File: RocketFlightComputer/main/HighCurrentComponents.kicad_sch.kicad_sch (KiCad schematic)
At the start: 31 parts, among them J1 BATT, Q2 SI2302, Q3 SI2302, Q4 SI2302

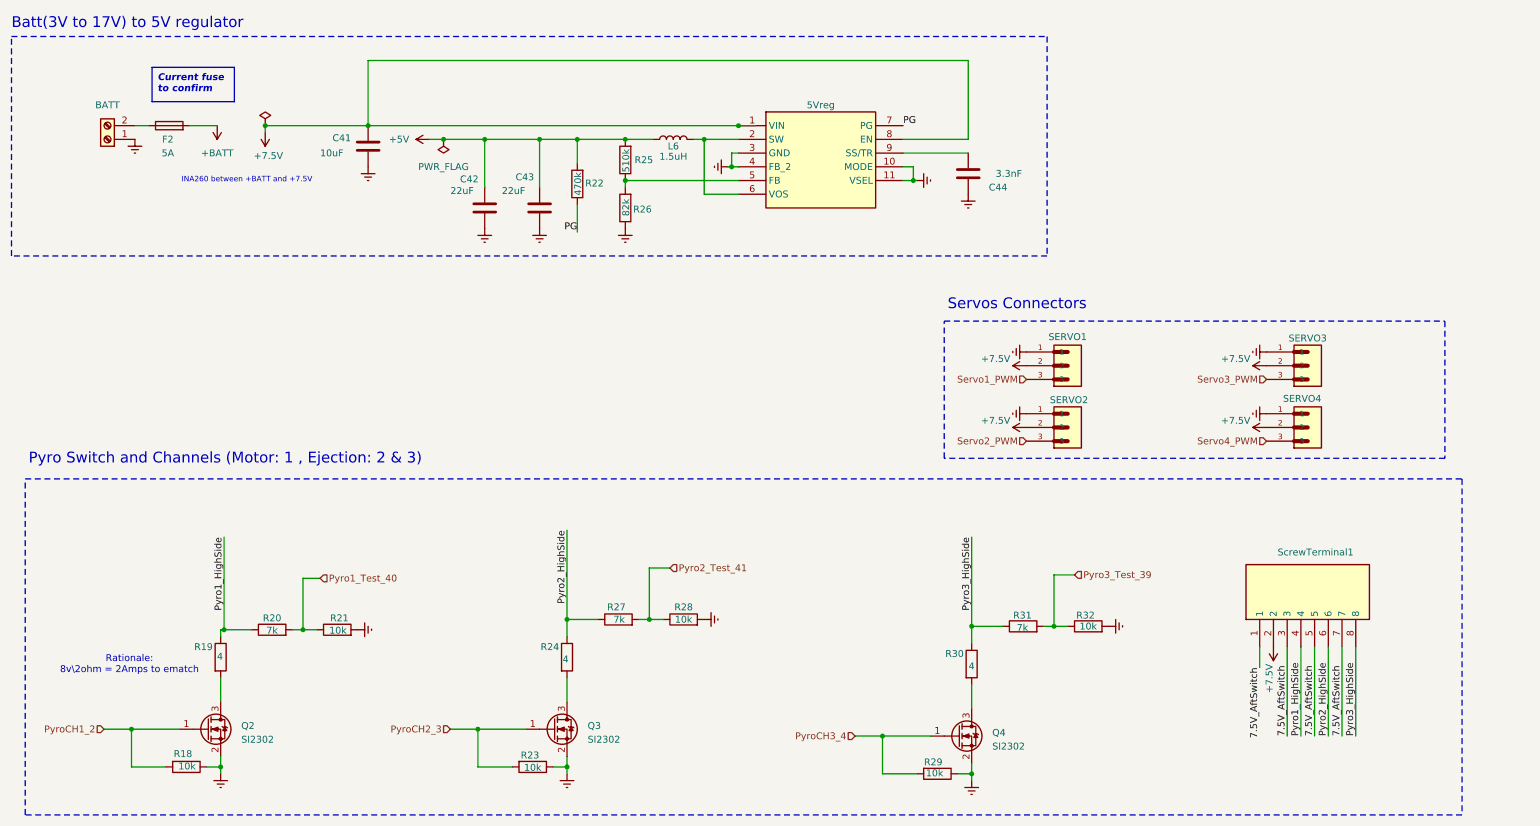
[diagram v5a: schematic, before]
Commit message: Addition of teensy example and milestone on routing completed, missing a few components to connect
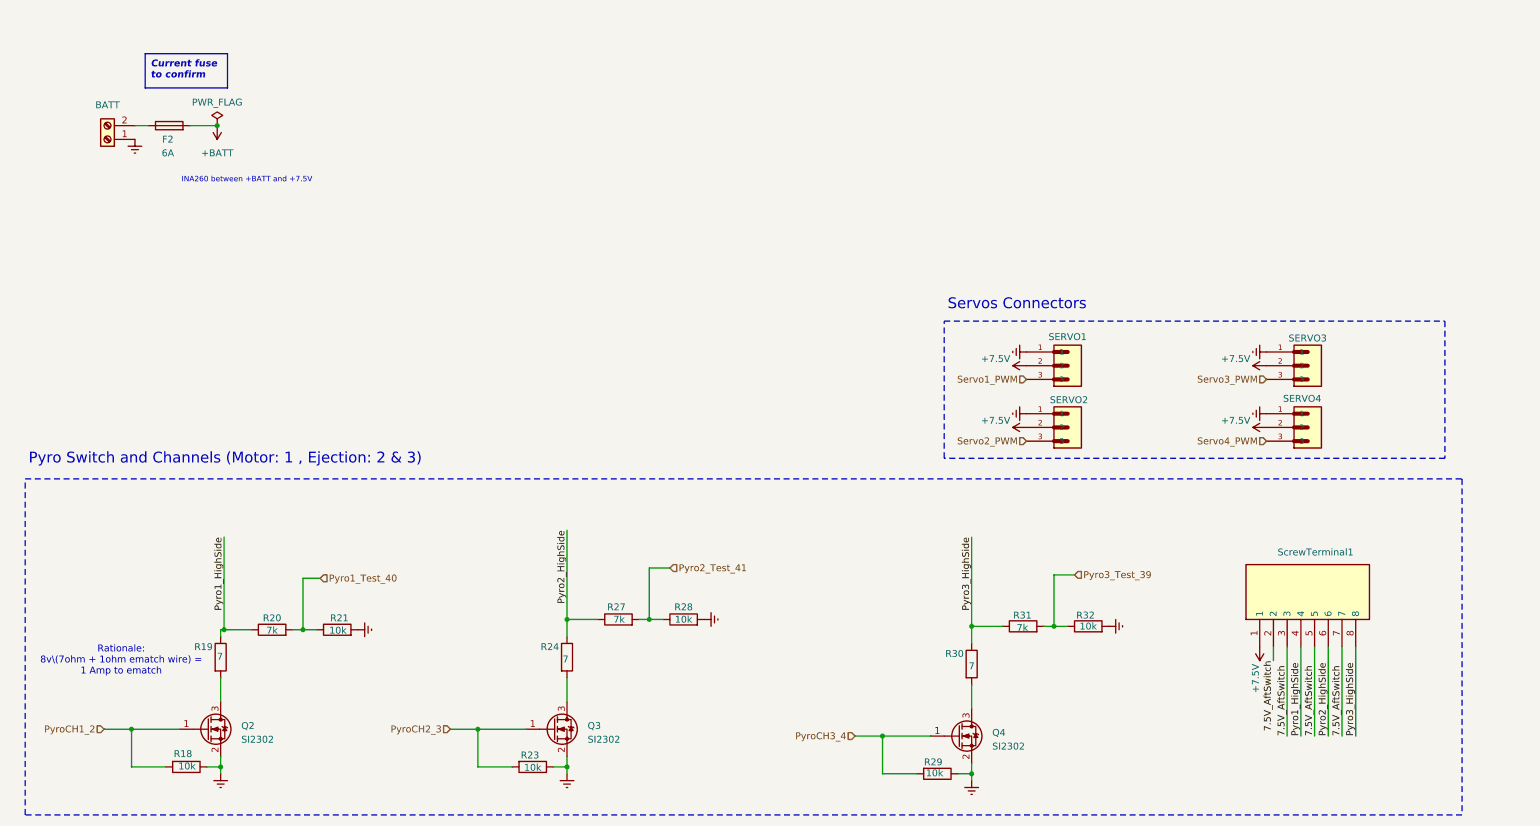
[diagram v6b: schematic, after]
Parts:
- removed C41: 10uF, Resistor_SMD:R_0603_1608Metric_Pad0.98x0.95mm_HandSolder, symbol Device:C
- removed C42, C43: 22uF, Resistor_SMD:R_0603_1608Metric_Pad0.98x0.95mm_HandSolder, symbol Device:C
- removed C44: 3.3nF, Resistor_SMD:R_0603_1608Metric_Pad0.98x0.95mm_HandSolder, symbol Device:C
- removed L6: 1.5uH, Resistor_SMD:R_0603_1608Metric_Pad0.98x0.95mm_HandSolder, symbol Device:L
- removed R22: 470k, Resistor_SMD:R_0603_1608Metric_Pad0.98x0.95mm_HandSolder, symbol Device:R
- removed R25: 510k, Resistor_SMD:R_0603_1608Metric_Pad0.98x0.95mm_HandSolder, symbol Device:R
- removed R26: 82k, Resistor_SMD:R_0603_1608Metric_Pad0.98x0.95mm_HandSolder, symbol Device:R
- removed TPS621361RGXT1: 5Vreg, footprint:TPS621361RGXT, symbol TPS621361RGXT:TPS621361RGXT
- F2: value 5A -> 6A; footprint Fuse:Fuse_0603_1608Metric -> Fuse:Fuse_1206_3216Metric
- R19, R24, R30: value 4 -> 7
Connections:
- net +7.5V: now also ScrewTerminal1.1; no longer ScrewTerminal1.2
- net 7.5V_AftSwitch: now also ScrewTerminal1.2; no longer ScrewTerminal1.1
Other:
- note added: "Rationale: 8v\(7ohm + 1ohm ematch wire) = 1 Amp to ematch"
- note removed: "Batt(3V to 17V) to 5V regulator"
- note removed: "Rationale: 8v\2ohm = 2Amps to ematch"

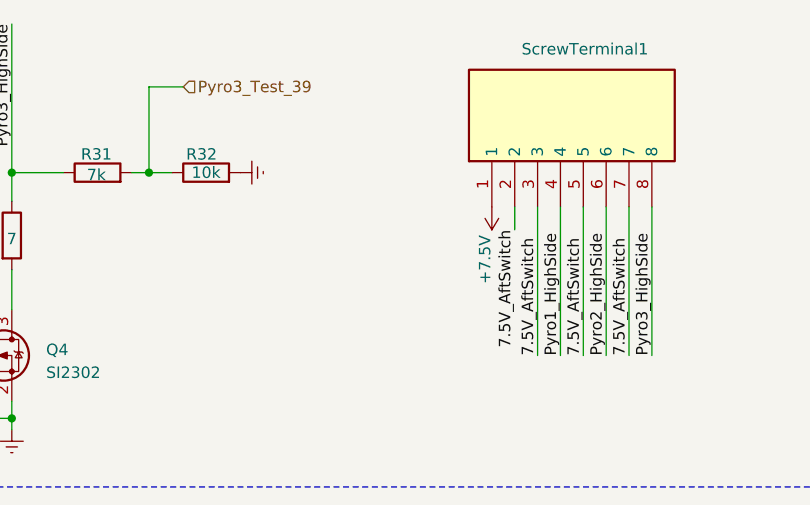
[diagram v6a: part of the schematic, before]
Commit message: Layout changes to incorporate power capacitors for the servos
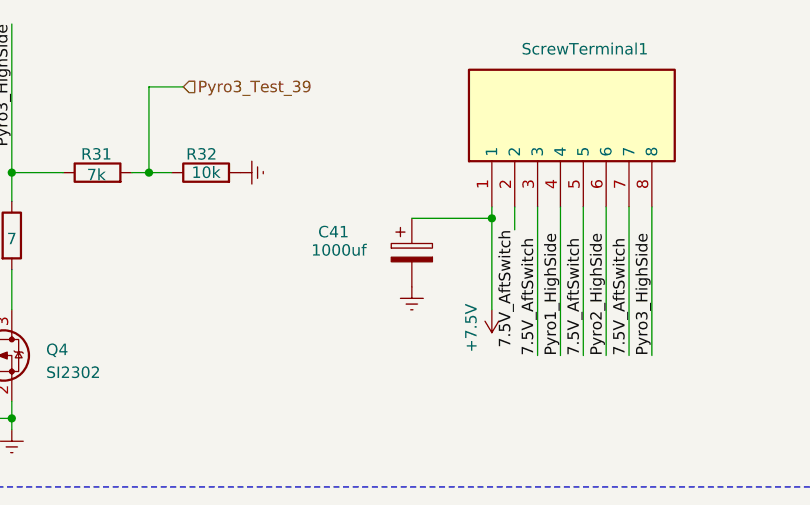
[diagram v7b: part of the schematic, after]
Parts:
- added C41: 1000uf, Capacitor_SMD:CP_Elec_5x5.8, symbol Device:C_Polarized
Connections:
- net +7.5V: now also C41.1
- net GNDREF: now also C41.2
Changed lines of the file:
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@@
 	)
 	(junction
+		(at 247.65 133.35)
+		(diameter 0)
+		(color 0 0 0 0)
+	)
+	(junction
 		(at 134.62 127)
 		(diameter 0)
@@
 	(wire
 		(pts
+			(xy 247.65 133.35) (xy 247.65 143.51)
+		)
+		(stroke
+			(width 0)
+			(type default)
+		)
+	)
+	(wire
+		(pts
 			(xy 119.38 110.49) (xy 119.38 127)
 		)
@@
 	(wire
 		(pts
+			(xy 238.76 133.35) (xy 247.65 133.35)
+		)
+		(stroke
+			(width 0)
+			(type default)
+		)
+	)
+	(wire
+		(pts
 			(xy 55.245 154.305) (xy 55.245 152.4)
 		)
@@
 	(wire
 		(pts
+			(xy 247.65 133.35) (xy 247.65 132.08)
+		)
+		(stroke
+			(width 0)
+			(type default)
+		)
+	)
+	(wire
+		(pts
 			(xy 250.19 132.08) (xy 250.19 134.62)
 		)
@@
 	)
 	(symbol
+		(lib_id "Device:C_Polarized")
+		(at 238.76 137.16 0)
+		(unit 1)
+		(exclude_from_sim no)
+		(in_bom yes)
+		(on_board yes)
+		(dnp no)
+		(property "Reference" "C41"
+			(at 228.346 134.874 0)
+			(effects
+				(font
+					(size 1.27 1.27)
+				)
+				(justify left)
+			)
+		)
+		(property "Value" "1000uf"
+			(at 227.584 136.906 0)
+			(effects
+				(font
+					(size 1.27 1.27)
+				)
+				(justify left)
+			)
+		)
+		(property "Footprint" "Capacitor_SMD:CP_Elec_5x5.8"
+			(at 239.7252 140.97 0)
+			(effects
+				(font
+					(size 1.27 1.27)
+				)
+				(hide yes)
+			)
+		)
+		(property "Datasheet" "~"
+			(at 238.76 137.16 0)
+			(effects
+				(font
+					(size 1.27 1.27)
+				)
+				(hide yes)
+			)
+		)
+		(property "Description" "Polarized capacitor, 16v"
+			(at 238.76 137.16 0)
+			(effects
+				(font
+					(size 1.27 1.27)
+				)
+				(hide yes)
+			)
+		)
+		(pin "2"
+		)
+		(pin "1"
+		)
+		(instances
+			(project ""
+				(path "/27195d1d-92b2-40df-ada5-3b20841577e7/03966d30-d016-427a-9db2-b49a5b43d133"
+					(reference "C41")
+					(unit 1)
+				)
+			)
+		)
+	)
+	(symbol
+		(lib_id "power:GNDREF")
+		(at 238.76 140.97 0)
+		(unit 1)
+		(exclude_from_sim no)
+		(in_bom yes)
+		(on_board yes)
+		(dnp no)
+		(fields_autoplaced yes)
+		(property "Reference" "#PWR097"
+			(at 238.76 147.32 0)
+			(effects
+				(font
+					(size 1.27 1.27)
+				)
+				(hide yes)
+			)
+		)
+		(property "Value" "GNDREF"
+			(at 238.125 144.78 90)
+			(effects
+				(font
+					(size 1.27 1.27)
+				)
+				(justify right)
+				(hide yes)
+			)
+		)
+		(property "Footprint" ""
+			(at 238.76 140.97 0)
+			(effects
+				(font
+					(size 1.27 1.27)
+				)
+				(hide yes)
+			)
+		)
+		(property "Datasheet" ""
+			(at 238.76 140.97 0)
+			(effects
+				(font
+					(size 1.27 1.27)
+				)
+				(hide yes)
+			)
+		)
+		(property "Description" ""
+			(at 238.76 140.97 0)
+			(effects
+				(font
+					(size 1.27 1.27)
+				)
+				(hide yes)
+			)
+		)
+		(pin "1"
+		)
+		(instances
+			(project "main"
+				(path "/27195d1d-92b2-40df-ada5-3b20841577e7/03966d30-d016-427a-9db2-b49a5b43d133"
+					(reference "#PWR097")
+					(unit 1)
+				)
+			)
+		)
+	)
+	(symbol
 		(lib_id "Device:R")
 		(at 140.97 127 90)
@@
 	(symbol
 		(lib_id "power:+7.5V")
-		(at 247.65 132.08 180)
+		(at 247.65 143.51 180)
 		(unit 1)
 		(exclude_from_sim no)
@@
 		(dnp no)
 		(property "Reference" "#PWR0149"
-			(at 247.65 128.27 0)
+			(at 247.65 139.7 0)
 			(effects
 				(font
@@
 		)
 		(property "Value" "+7.5V"
-			(at 246.888 137.922 90)
+			(at 245.364 145.542 90)
 			(effects
 				(font
@@
 		)
 		(property "Footprint" ""
-			(at 247.65 132.08 0)
+			(at 247.65 143.51 0)
 			(effects
 				(font
@@
 		)
 		(property "Datasheet" ""
-			(at 247.65 132.08 0)
+			(at 247.65 143.51 0)
 			(effects
 				(font
@@
 		)
 		(property "Description" ""
-			(at 247.65 132.08 0)
+			(at 247.65 143.51 0)
 			(effects
 				(font

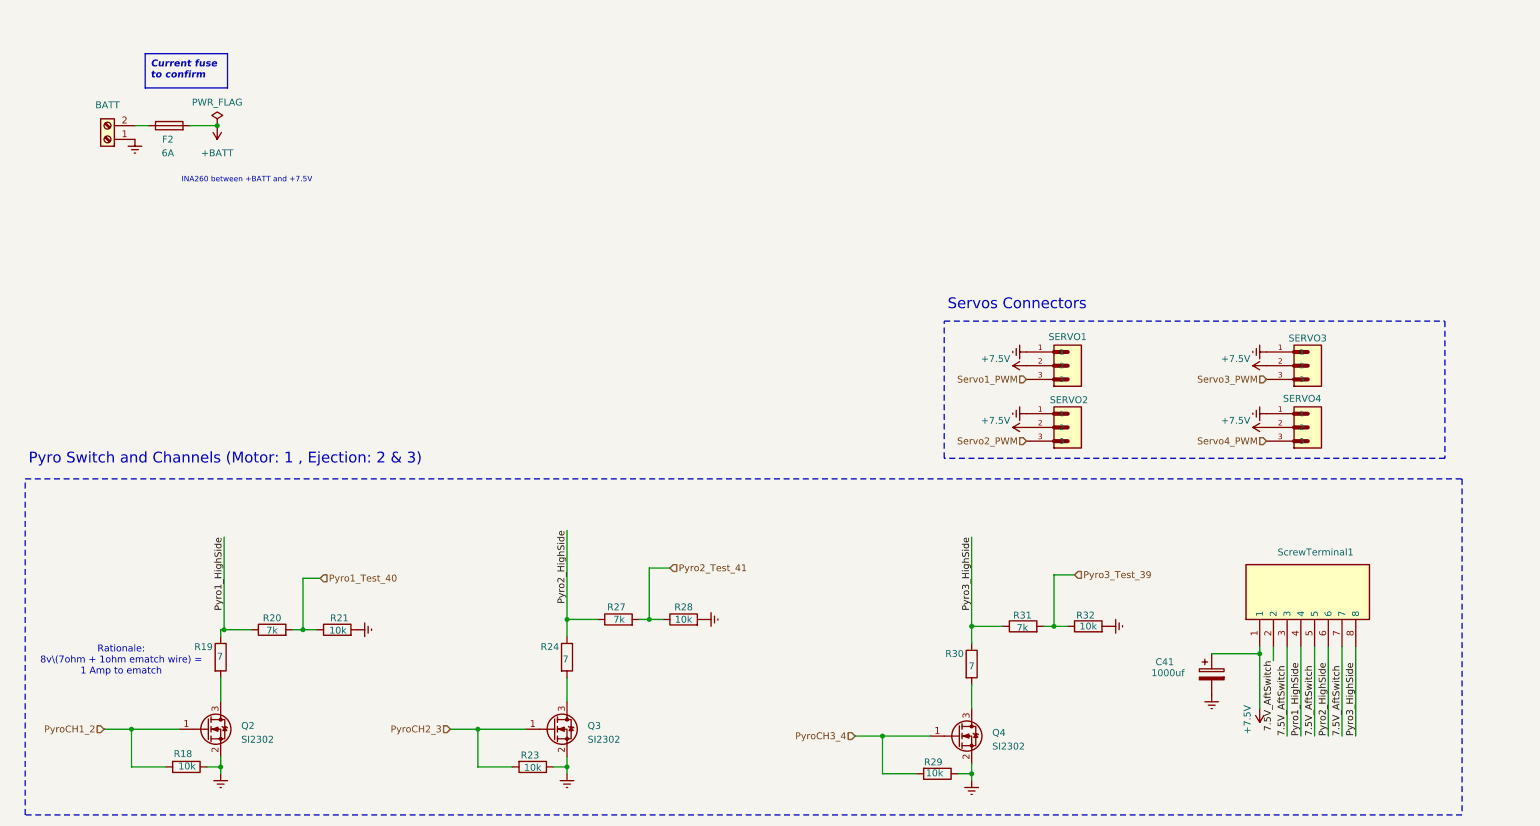
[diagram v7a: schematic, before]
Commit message: Addition of all components in BOM, metal mounting plates, need to check psram if its ok for signals to pass under, all components need a double check
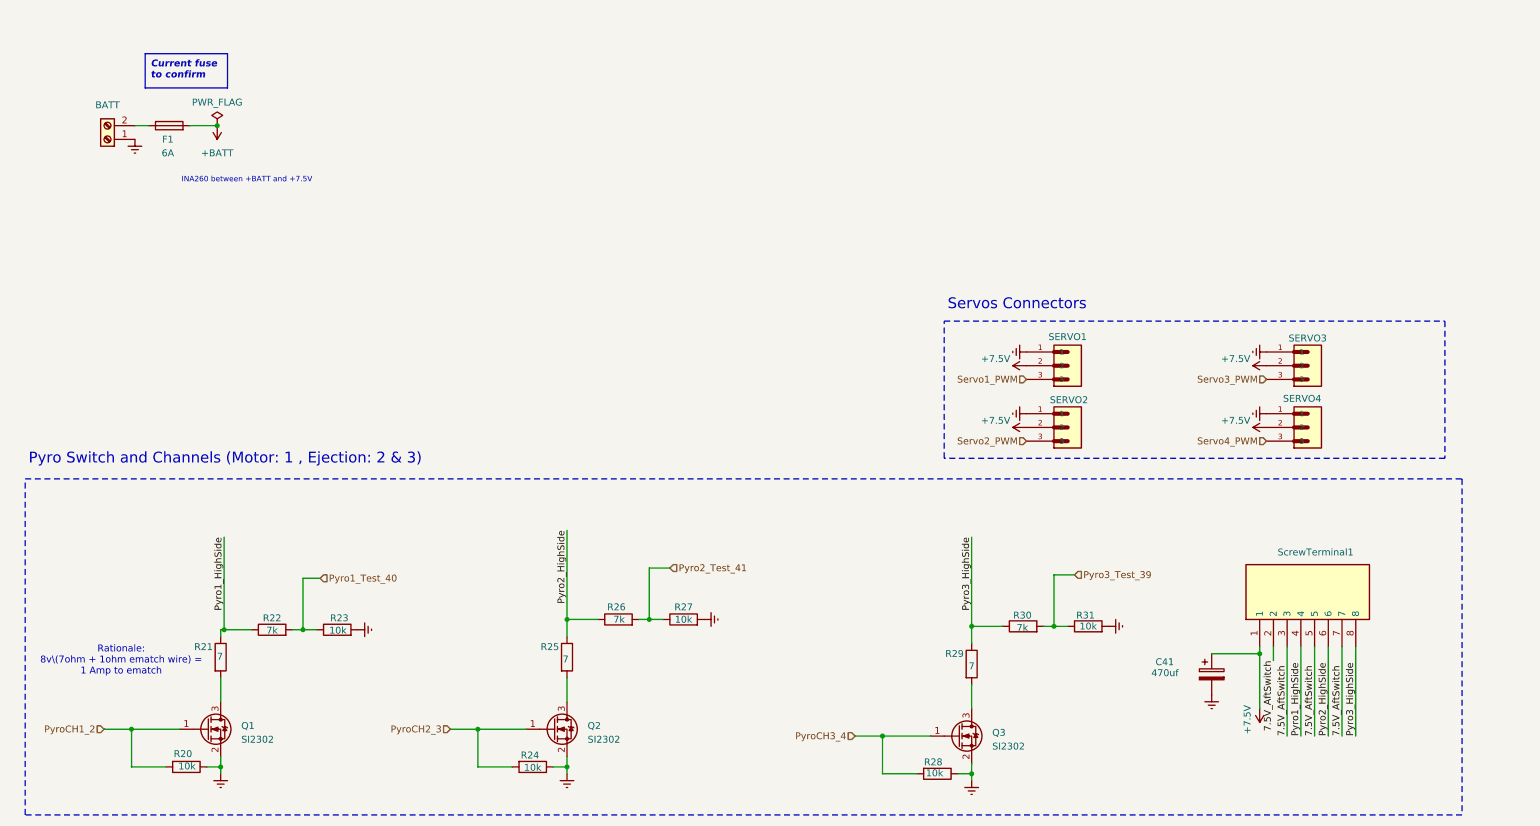
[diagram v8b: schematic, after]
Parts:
- C41: value 1000uf -> 470uf; footprint Capacitor_SMD:CP_Elec_5x5.8 -> Capacitor_THT:C_Radial_D6.3mm_H11.0mm_P2.50mm; LCSC (none) -> C1020067
- F1: renamed from F2; LCSC (none) -> C183157; Mouser Part Number (none) -> 530-C1F6
- Q1: renamed from Q2; LCSC (none) -> C460978; Mouser Part Number (none) -> 621-DMG3406L-7
- Q2: renamed from Q3; LCSC (none) -> C460978; Mouser Part Number (none) -> 621-DMG3406L-7
- Q3: renamed from Q4; LCSC (none) -> C460978; Mouser Part Number (none) -> 621-DMG3406L-7
- R20: renamed from R18; LCSC (none) -> C25804
- R21: renamed from R19; LCSC (none) -> C228062
- R22: renamed from R20; LCSC (none) -> C23101
- R23: renamed from R21; LCSC (none) -> C25804
- R24: renamed from R23; LCSC (none) -> C25804
- R25: renamed from R24; LCSC (none) -> C228062
- R26: renamed from R27; LCSC (none) -> C23101
- R27: renamed from R28; LCSC (none) -> C25804
- R28: renamed from R29; LCSC (none) -> C25804
- R29: renamed from R30; LCSC (none) -> C228062
- R30: renamed from R31; LCSC (none) -> C23101
- R31: renamed from R32; LCSC (none) -> C25804
- SERVO1, SERVO2, SERVO3, SERVO4: LCSC (none) -> C161691; Mouser Part Number (none) -> 306-BM03BGHSTBTLFSNN
- ScrewTerminal1: LCSC (none) -> C5476987
- ScrewTerminal2: renamed from J1; LCSC (none) -> C3029316; Mouser Part Number (none) -> 651-1725656
